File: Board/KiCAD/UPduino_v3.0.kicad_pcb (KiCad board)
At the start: 4 copper layers, 62 x 22.2 mm, 116 parts, among them J1 47589-0001, J2 Right, J3 Left, J4 5V Power, U1 93LC56BT-I/OT, U2 ICE40UP5K-SG48ITR, U3 FT232H, U4 SG-210STF 12.0000ML3, U5 W25Q32JVSSIM, U6 AP2127K-3.3, U7 AP2127K-1.2, U8 SN74AUP2G125DCUR

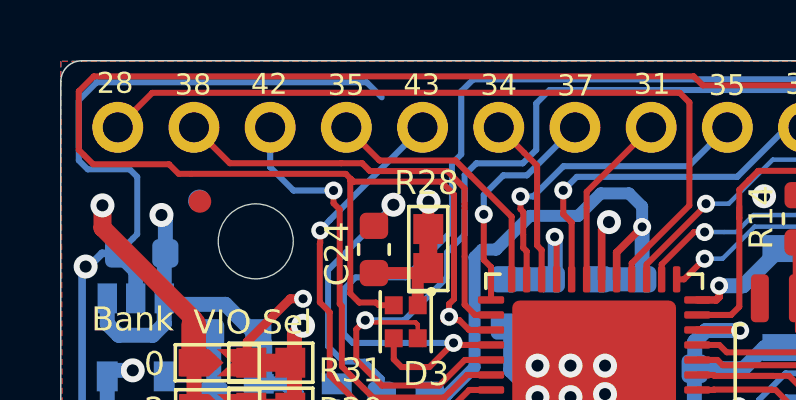
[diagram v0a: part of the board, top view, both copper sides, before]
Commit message: Update UPduino_v3.0.kicad_pcb
Fixed duplicate silkscreen (pin 35->36) on IOT48B connection
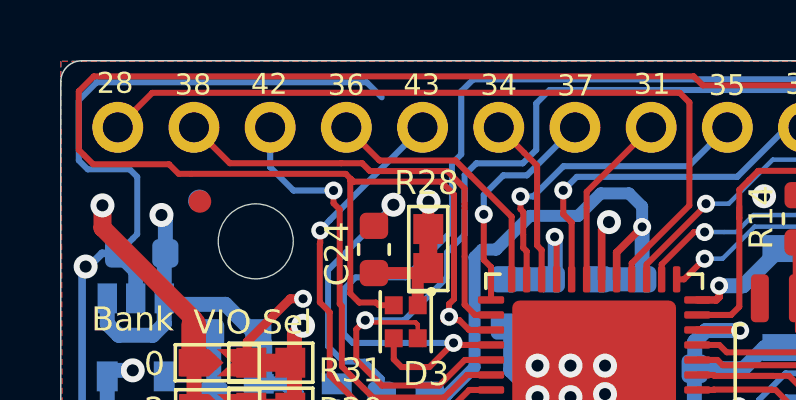
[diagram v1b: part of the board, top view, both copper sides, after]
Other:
- board text added: "36"
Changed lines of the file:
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@@
     (effects (font (size 0.7 0.7) (thickness 0.127)) (justify mirror))
   )
-  (gr_text 35 (at 109.47 78.56) (layer B.SilkS)
+  (gr_text 36 (at 109.47 78.56) (layer B.SilkS)
     (effects (font (size 0.7 0.7) (thickness 0.127)) (justify mirror))
   )
@@
     (effects (font (size 0.7 0.7) (thickness 0.127)))
   )
-  (gr_text 35 (at 109.51 78.59) (layer F.SilkS)
-    (effects (font (size 0.7 0.7) (thickness 0.127)))
-  )
+  (gr_text 36 (at 109.51 78.59) (layer F.SilkS)
+    (effects (font (size 0.7 0.7) (thickness 0.127)))
+  )
